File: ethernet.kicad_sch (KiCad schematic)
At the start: 39 parts, among them IC601 ACPL-217-500E, J601 5-2337992-8, U601 TPS2372-3RGWR, U602 ULS-12{slash}5-D48N-C

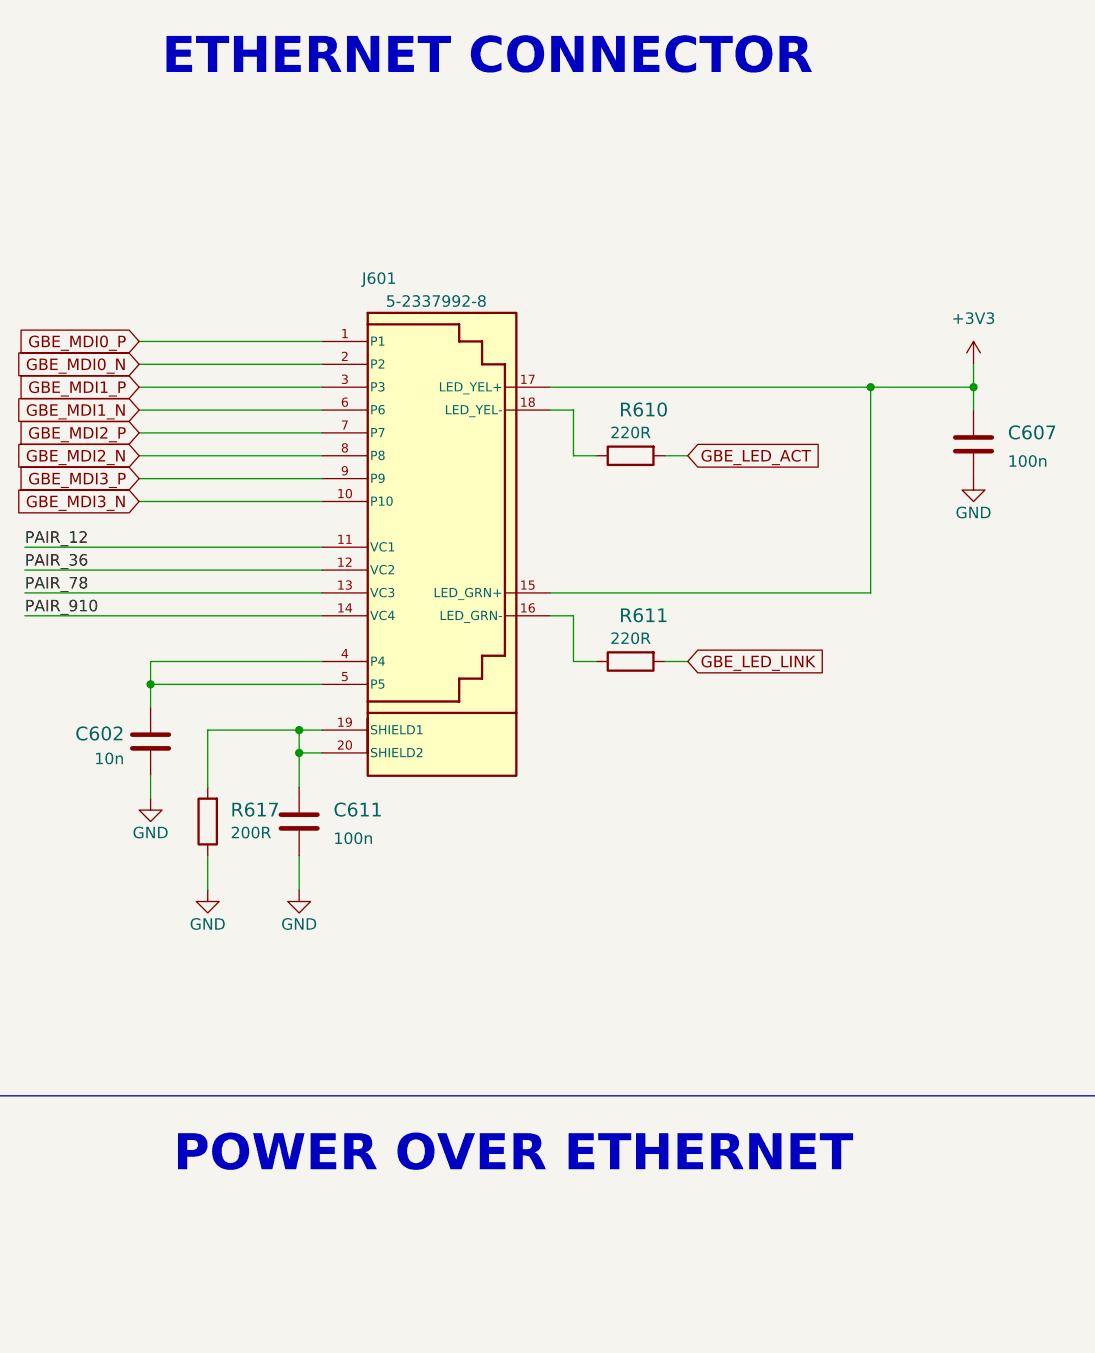
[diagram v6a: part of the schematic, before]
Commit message: Cleaned up schematic after project changes
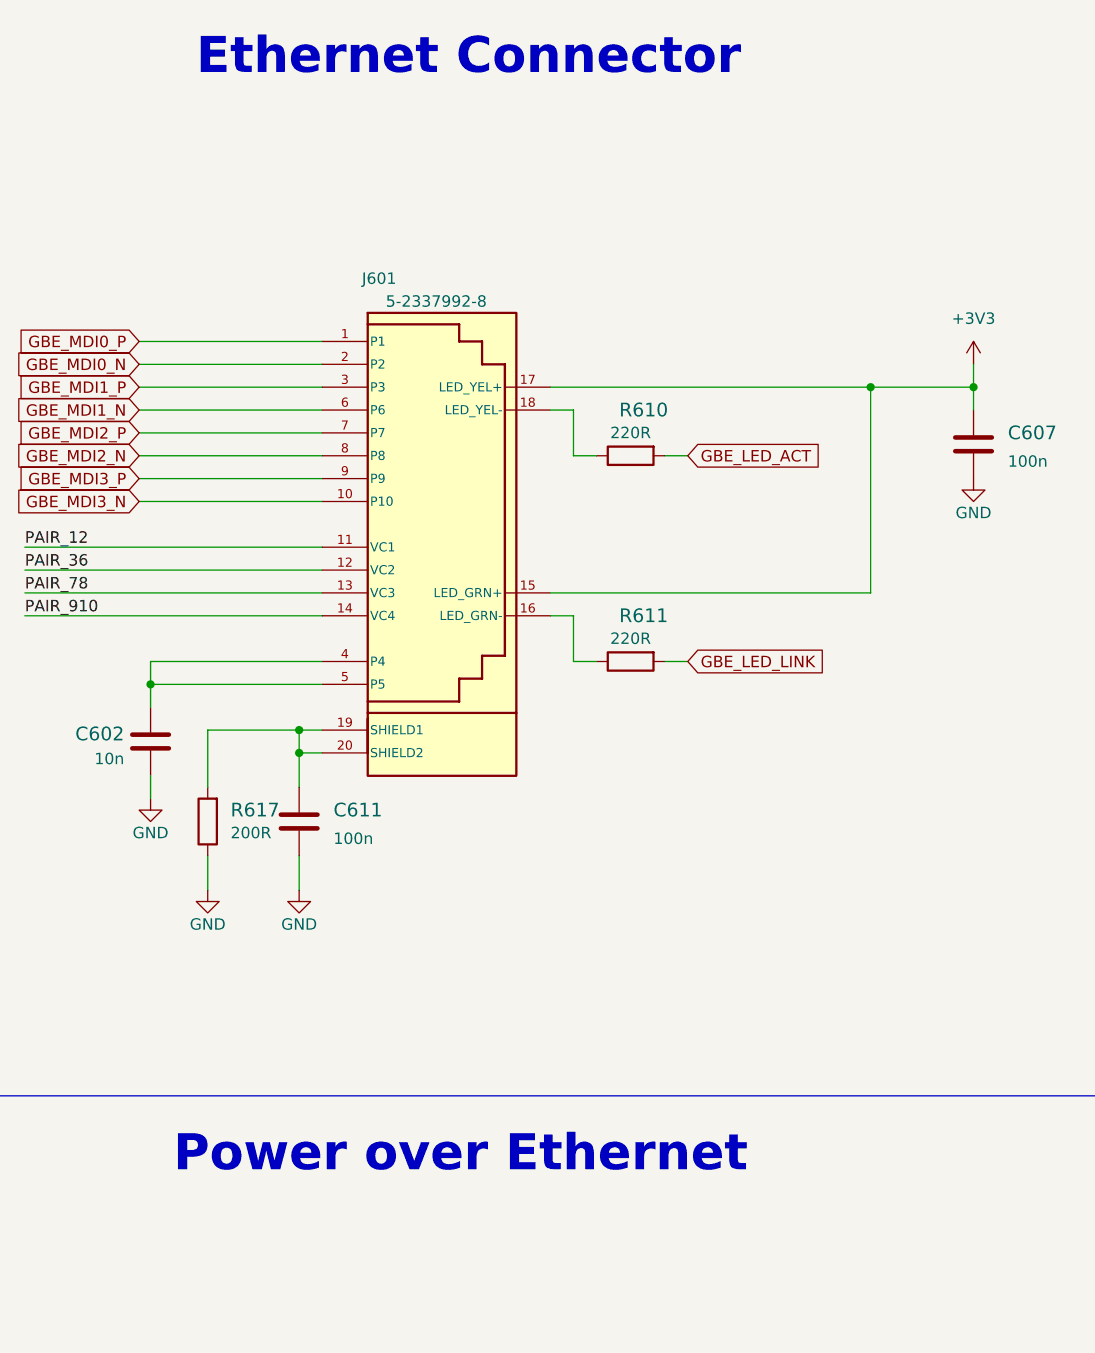
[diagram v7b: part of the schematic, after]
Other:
- note added: "Ethernet Connector"
- note added: "Power over Ethernet"
- note removed: "ETHERNET CONNECTOR"
- note removed: "POWER OVER ETHERNET"
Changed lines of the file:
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@@
     )
   )
-  (text "POWER OVER ETHERNET" (at 168.91 143.51 0)
+  (text "Power over Ethernet" (at 168.91 143.51 0)
     (effects (font (size 4 4) (thickness 0.5994) bold) (justify left bottom))
   )
-  (text "ETHERNET CONNECTOR" (at 167.64 21.59 0)
+  (text "Ethernet Connector" (at 171.45 21.59 0)
     (effects (font (size 4 4) (thickness 0.5994) bold) (justify left bottom))
   )

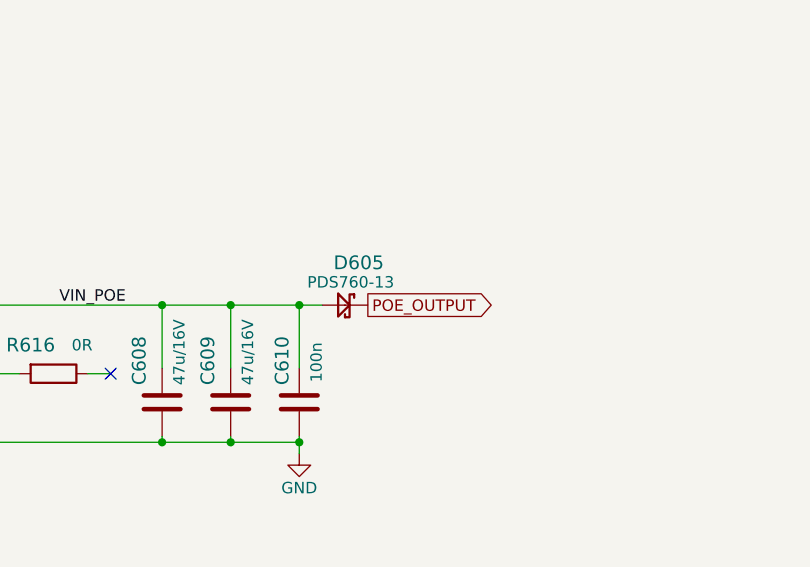
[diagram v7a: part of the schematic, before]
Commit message: Added power switches and selectors, added standby LDO
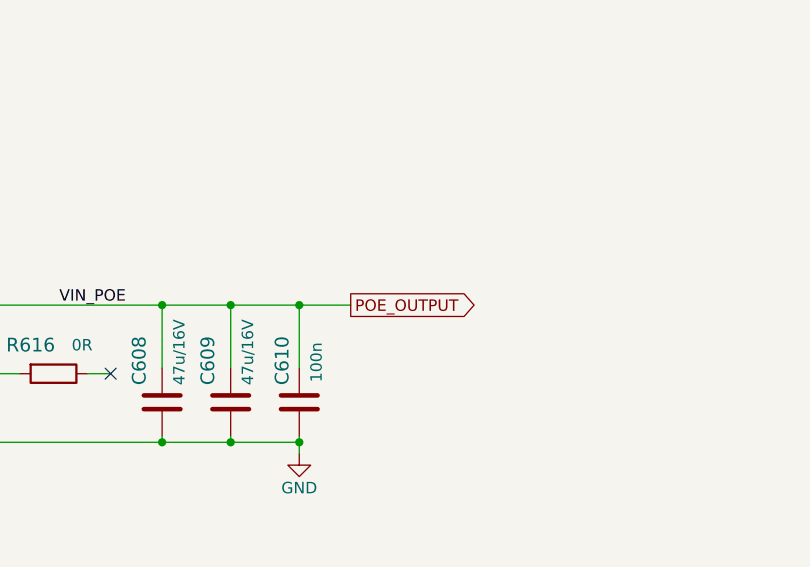
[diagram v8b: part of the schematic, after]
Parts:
- removed D605: PDS760-13, antmicro-footprints:PDS760-13, symbol antmicroDiodesRectifiersSingle:PDS760-13
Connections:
- net VIN_POE is gone; now on net POE_OUTPUT: C608.1, C609.1, C610.1, U602.7 (SENSE+), U602.8 (VOUT+)
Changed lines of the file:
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@@
   (junction (at 131.445 217.17) (diameter 0) (color 0 0 0 0)
   )
-  (junction (at 339.725 181.61) (diameter 0) (color 0 0 0 0)
-  )
   (junction (at 246.38 55.88) (diameter 0) (color 0 0 0 0)
   )
@@
   (junction (at 205.74 181.61) (diameter 0) (color 0 0 0 0)
   )
+  (junction (at 339.725 181.61) (diameter 0) (color 0 0 0 0)
+  )
   (no_connect (at 193.675 210.82))
   (no_connect (at 193.675 223.52))
@@
     (stroke (width 0) (type default) (color 0 0 0 0))
   )
-  (wire (pts (xy 339.725 181.61) (xy 342.265 181.61))
-    (stroke (width 0) (type default) (color 0 0 0 0))
-  )
   (wire (pts (xy 223.52 86.36) (xy 226.06 86.36))
     (stroke (width 0) (type default) (color 0 0 0 0))
@@
     (stroke (width 0) (type default) (color 0 0 0 0))
   )
+  (wire (pts (xy 339.725 181.61) (xy 345.44 181.61))
+    (stroke (width 0) (type default) (color 0 0 0 0))
+  )
   (wire (pts (xy 131.445 212.09) (xy 144.145 212.09))
     (stroke (width 0) (type default) (color 0 0 0 0))
@@
     )
   )
-  (global_label "POE_OUTPUT" (shape output) (at 347.345 181.61 0)
+  (global_label "POE_OUTPUT" (shape output) (at 345.44 181.61 0)
     (effects (font (size 1.27 1.27)) (justify left))
-    (property "Intersheet References" "${INTERSHEET_REFS}" (id 0) (at 362.585 181.61 0)
+    (property "Intersheet References" "${INTERSHEET_REFS}" (id 0) (at 360.68 181.61 0)
       (effects (font (size 1.27 1.27)) (justify left))
     )
@@
     (pin "1")
   )
-  (symbol (lib_id "antmicroDiodesRectifiersSingle:PDS760-13") (at 344.805 181.61 270) (unit 1)
-    (in_bom yes) (on_board yes)
-    (property "Reference" "D605" (id 0) (at 343.535 177.8 90)
-      (effects (font (size 1.524 1.524)) (justify left bottom))
-    )
-    (property "Value" "PDS760-13" (id 1) (at 342.773 184.15 0)
-      (effects (font (size 1.27 1.27)) (justify left bottom) hide)
-    )
-    (property "Footprint" "antmicro-footprints:PDS760-13" (id 2) (at 330.073 181.356 0)
-      (effects (font (size 1.27 1.27)) hide)
-    )
-    (property "Datasheet" "" (id 3) (at 344.805 181.61 0)
-      (effects (font (size 1.524 1.524)) hide)
-    )
-    (property "Manufacturer" "Diodes Inc." (id 4) (at 342.011 189.484 0)
-      (effects (font (size 1.27 1.27)) hide)
-    )
-    (property "MPN" "PDS760-13" (id 5) (at 345.44 179.07 90))
-    (pin "A")
-    (pin "C")
-  )
   (symbol (lib_id "power:GNDD") (at 265.43 209.55 0) (unit 1)
